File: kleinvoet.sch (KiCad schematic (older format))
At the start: 35 parts, among them CN1 Conn_01x06, CN2 Conn_01x10, CN3 Conn_01x08, J1 Conn_ST_STDC14, SW1 RESET, U1 STM32F446RETx, U2 W25Q128JVS, Y1 12 MHz, Y2 32.768 kHz

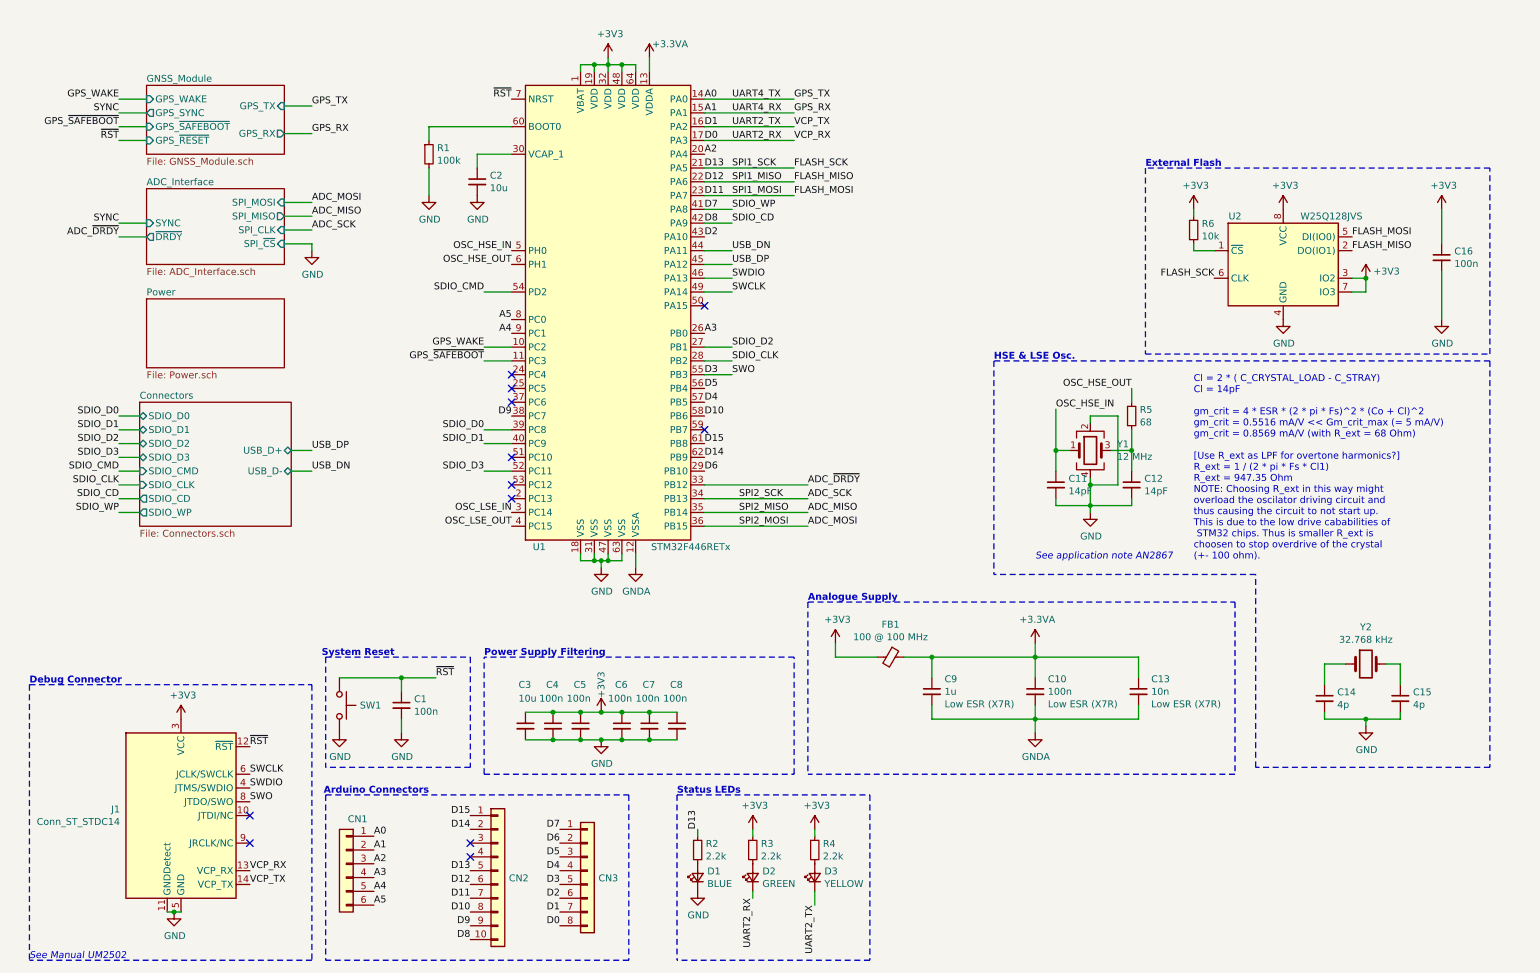
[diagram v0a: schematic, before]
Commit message: Assign footprints for all components
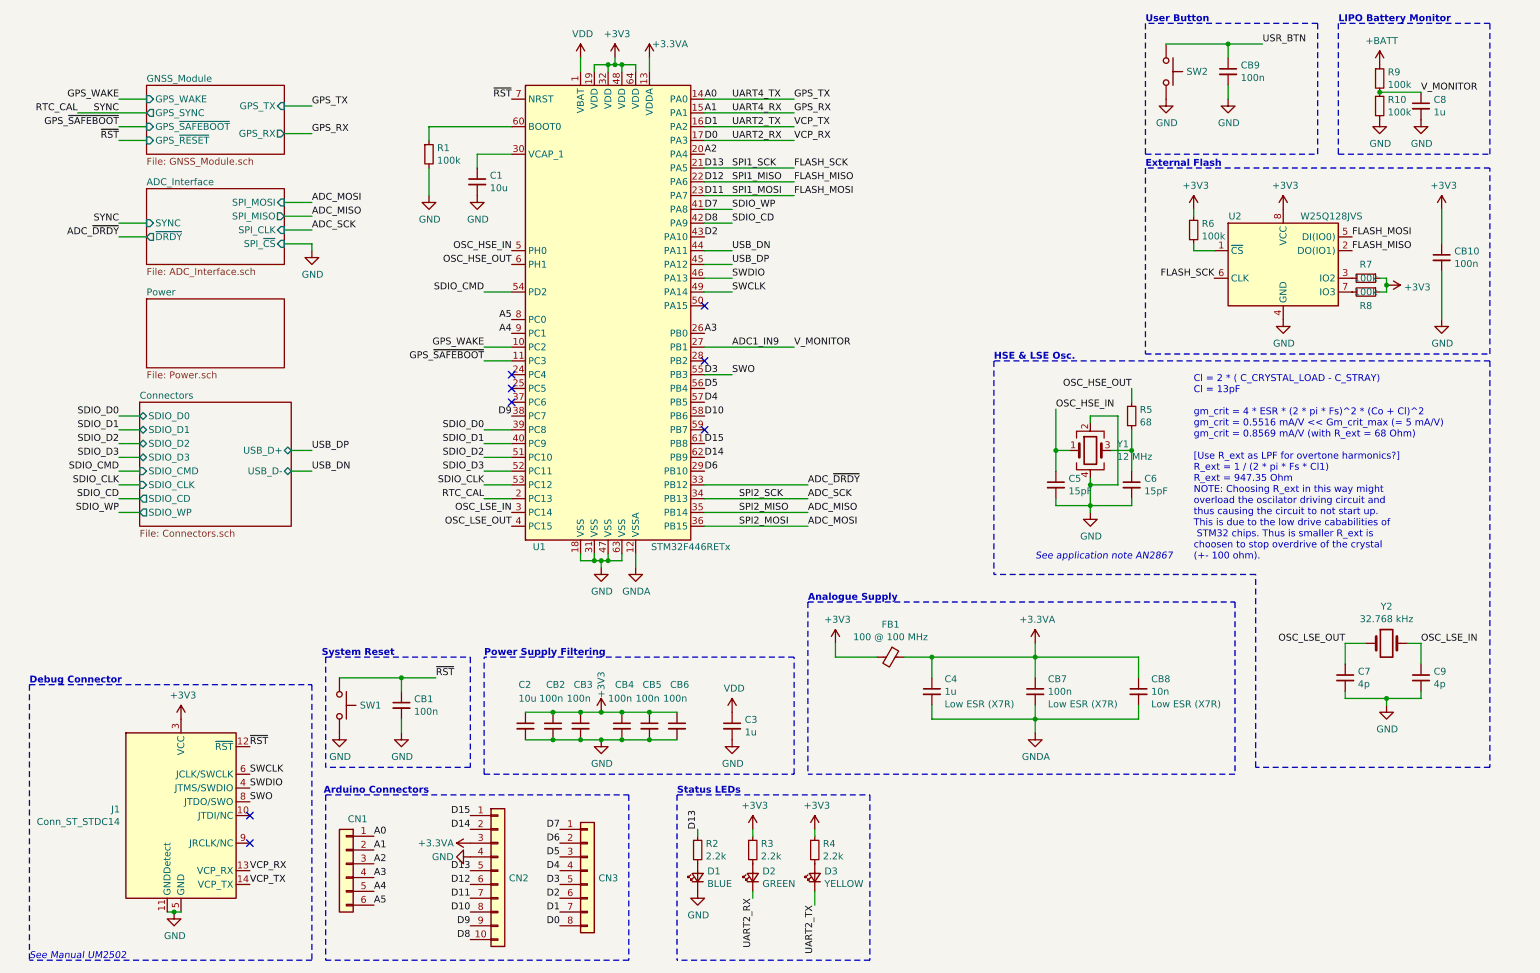
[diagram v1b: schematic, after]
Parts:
- added C3, C8: 1u, Capacitor_SMD:C_0603_1608Metric_Pad1.05x0.95mm_HandSolder, symbol Device:C_Small
- added CB9: 100n, Capacitor_SMD:C_0603_1608Metric_Pad1.05x0.95mm_HandSolder, symbol Device:C_Small
- added R10, R7, R8, R9: 100k, Resistor_SMD:R_0603_1608Metric_Pad1.05x0.95mm_HandSolder, symbol Device:R_Small
- added SW2: RESET, grootvoet:SW_SPST_PTS647, symbol Switch:SW_Push
- C1: renamed from C2; footprint (none) -> Capacitor_SMD:C_0805_2012Metric_Pad1.15x1.40mm_HandSolder; MPN (none) -> C0805C106K9PACTU; Mfr. (none) -> KEMET
- C2: renamed from C3; footprint (none) -> Capacitor_SMD:C_0805_2012Metric_Pad1.15x1.40mm_HandSolder; MPN (none) -> C0805C106K9PACTU; Mfr. (none) -> KEMET
- C4: renamed from C9; footprint (none) -> Capacitor_SMD:C_0603_1608Metric_Pad1.05x0.95mm_HandSolder; MPN (none) -> C0603C105K8RACTU; Mfr. (none) -> KEMET
- C5: renamed from C11; value 14pF -> 15pF; footprint (none) -> Capacitor_SMD:C_0603_1608Metric_Pad1.05x0.95mm_HandSolder; MPN (none) -> C0603C150J5GACTU; Mfr. (none) -> KEMET
- C6: renamed from C12; value 14pF -> 15pF; footprint (none) -> Capacitor_SMD:C_0603_1608Metric_Pad1.05x0.95mm_HandSolder; MPN (none) -> C0603C150J5GACTU; Mfr. (none) -> KEMET
- C7: renamed from C14; footprint (none) -> Capacitor_SMD:C_0603_1608Metric_Pad1.05x0.95mm_HandSolder; MPN (none) -> C1608C0G1H040C080AA; Mfr. (none) -> TDK
- C9: renamed from C15; footprint (none) -> Capacitor_SMD:C_0603_1608Metric_Pad1.05x0.95mm_HandSolder; MPN (none) -> C1608C0G1H040C080AA; Mfr. (none) -> TDK
- CB1: renamed from C1; footprint (none) -> Capacitor_SMD:C_0603_1608Metric_Pad1.05x0.95mm_HandSolder; MPN (none) -> C0603C104M5RACTU; Mfr. (none) -> KEMET
- CB10: renamed from C16; footprint (none) -> Capacitor_SMD:C_0603_1608Metric_Pad1.05x0.95mm_HandSolder; MPN (none) -> C0603C104M5RACTU; Mfr. (none) -> KEMET
- CB2: renamed from C4; footprint (none) -> Capacitor_SMD:C_0603_1608Metric_Pad1.05x0.95mm_HandSolder; MPN (none) -> C0603C104M5RACTU; Mfr. (none) -> KEMET
- CB3: renamed from C5; footprint (none) -> Capacitor_SMD:C_0603_1608Metric_Pad1.05x0.95mm_HandSolder; MPN (none) -> C0603C104M5RACTU; Mfr. (none) -> KEMET
- CB4: renamed from C6; footprint (none) -> Capacitor_SMD:C_0603_1608Metric_Pad1.05x0.95mm_HandSolder; MPN (none) -> C0603C104M5RACTU; Mfr. (none) -> KEMET
- CB5: renamed from C7; footprint (none) -> Capacitor_SMD:C_0603_1608Metric_Pad1.05x0.95mm_HandSolder; MPN (none) -> C0603C104M5RACTU; Mfr. (none) -> KEMET
- CB6: renamed from C8; footprint (none) -> Capacitor_SMD:C_0603_1608Metric_Pad1.05x0.95mm_HandSolder; MPN (none) -> C0603C104M5RACTU; Mfr. (none) -> KEMET
- CB7: renamed from C10; footprint (none) -> Capacitor_SMD:C_0603_1608Metric_Pad1.05x0.95mm_HandSolder; MPN (none) -> C0603C104M5RACTU; Mfr. (none) -> KEMET
- CB8: renamed from C13; footprint (none) -> Capacitor_SMD:C_0603_1608Metric_Pad1.05x0.95mm_HandSolder; MPN (none) -> C0603C103J5RACTU; Mfr. (none) -> KEMET
- CN1: footprint (none) -> Connector_PinHeader_2.54mm:PinHeader_1x06_P2.54mm_Vertical
- CN2: footprint (none) -> Connector_PinHeader_2.54mm:PinHeader_1x10_P2.54mm_Vertical
- CN3: footprint (none) -> Connector_PinHeader_2.54mm:PinHeader_1x08_P2.54mm_Vertical
- D1: footprint (none) -> LED_SMD:LED_0603_1608Metric_Pad1.05x0.95mm_HandSolder; MPN (none) -> SMLD12BN1WT86; Mfr. (none) -> ROHM Semiconductor
- D2: footprint (none) -> LED_SMD:LED_0603_1608Metric_Pad1.05x0.95mm_HandSolder;  MPN (none) -> SMLD12EN1WT86; Mfr. (none) -> ROHM Semiconductor
- D3: footprint (none) -> LED_SMD:LED_0603_1608Metric_Pad1.05x0.95mm_HandSolder; MPN (none) -> SML-D12Y8WT86C; Mfr. (none) -> ROHM Semiconductor
- FB1: footprint (none) -> Inductor_SMD:L_0603_1608Metric_Pad1.05x0.95mm_HandSolder; MPN (none) -> BLM18KG101TZ1D; Mfr. (none) -> Murata Semiconductor
- J1: footprint (none) -> Connector_PinHeader_1.27mm:PinHeader_2x07_P1.27mm_Vertical; MPN (none) -> M50-055023W0445; Mfr. (none) -> Harwin
- R1: footprint (none) -> Resistor_SMD:R_0603_1608Metric_Pad1.05x0.95mm_HandSolder; MPN (none) -> RC0603FR-07100KL; Mfr. (none) -> Yageo
- R2: footprint (none) -> Resistor_SMD:R_0603_1608Metric_Pad1.05x0.95mm_HandSolder; MPN (none) -> RC0603FR-072K2L; Mfr. (none) -> Yageo
- R3: footprint (none) -> Resistor_SMD:R_0603_1608Metric_Pad1.05x0.95mm_HandSolder; MFN (none) -> RC0603FR-072K2L; Mfr. (none) -> Yageo
- R4: footprint (none) -> Resistor_SMD:R_0603_1608Metric_Pad1.05x0.95mm_HandSolder
- R5: footprint (none) -> Resistor_SMD:R_0603_1608Metric_Pad1.05x0.95mm_HandSolder; MPN (none) -> RC0603FR-1068RL; Mfr. (none) -> Yageo
- R6: value 10k -> 100k; footprint (none) -> Resistor_SMD:R_0603_1608Metric_Pad1.05x0.95mm_HandSolder; MPN (none) -> RC0603FR-07100KL; Mfr. (none) -> Yageo
- SW1: footprint (none) -> grootvoet:SW_SPST_PTS647; MPN (none) -> PTS647SN50SMTR2LFS; Mfr. (none) -> C&K
- U2: footprint Package_SO:SOIC-8_5.23x5.23mm_P1.27mm -> grootvoet:SOIC-8_5.23x5.23mm_P1.27mm
- Y1: footprint (none) -> grootvoet:ECS-33B; Mfr. (none) -> ECS
- Y2: footprint (none) -> grootvoet:ECX-31B
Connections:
- net +3.3VA: now also CN2.3 (Pin_3)
- net +3V3: now also R7.1, R8.1; no longer U1.1 (VBAT), U2.3 (IO2), U2.7 (IO3)
- net GND: now also CN2.4 (Pin_4), C3.2, C8.2, CB9.2, R10.2, SW2.2
- net OSC_LSE_IN: now also C9.1, Y2.2
- net OSC_LSE_OUT: now also C7.1, Y2.1
- net SDIO_CLK: now also U1.53 (PC12); no longer U1.28 (PB2)
- net SDIO_D2: now also U1.51 (PC10); no longer U1.27 (PB1)
- net RTC_CAL: now reaches U1.2 (PC13)
- new net: R7.2, U2.3 (IO2)
- new net: R8.2, U2.7 (IO3)
- new net +BATT: R9.1
- new net ADC1_IN9: C8.1, R10.1, R9.2, U1.27 (PB1)
- new net USR_BTN: CB9.1, SW2.1
- new net VDD: C3.1, U1.1 (VBAT)
- no-connect marks 12 -> 8
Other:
- note added: "Cl = 2 * ( C_CRYSTAL_LOAD - C_STRAY)\nCl = 13pF\n\ngm_crit = 4 * ESR * (2 * pi * Fs)^2 * (Co + Cl)^2\ngm_crit = 0.5516 mA/V << Gm_crit_max (= 5 mA/V)\ngm_crit = 0.8569 mA/V (with R_ext = 68 Ohm)\n\n[Use R_ext as LPF for overtone harmonics?]\nR_ext = 1 / (2 * pi * Fs * Cl1)\nR_ext = 947.35 Ohm\nNOTE: Choosing R_ext in this way might \noverload the oscilator driving circuit and \nthus causing the c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"
- note added: "LIPO Battery Monitor"
- note added: "User Button"
- note removed: "Cl = 2 * ( C_CRYSTAL_LOAD - C_STRAY)\nCl = 14pF\n\ngm_crit = 4 * ESR * (2 * pi * Fs)^2 * (Co + Cl)^2\ngm_crit = 0.5516 mA/V << Gm_crit_max (= 5 mA/V)\ngm_crit = 0.8569 mA/V (with R_ext = 68 Ohm)\n\n[Use R_ext as LPF for overtone harmonics?]\nR_ext = 1 / (2 * pi * Fs * Cl1)\nR_ext = 947.35 Ohm\nNOTE: Choosing R_ext in this way might \noverload the oscilator driving circuit and \nthus causing the c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"
- moved on the sheet: C7, C9, Y2

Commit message: Change Mic Preamp
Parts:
- C3, C8: MPN (none) -> C0603C105K8RACTU; Mfr. (none) -> KEMET
- D2:  MPN SMLD12EN1WT86 -> (none); MPN (none) -> SMLD12EN1WT86
- FB1: value Ferrite_Bead_Small -> BLM18KG101TZ1D; Mfr. Murata Semiconductor -> Murata Electronics
- R3: MFN RC0603FR-072K2L -> (none); MPN (none) -> RC0603FR-072K2L
- R4: MPN (none) -> RC0603FR-072K2L; Mfr. (none) -> Yageo
- R7: MFN RC0603FR-07100KL -> (none); MPN (none) -> RC0603FR-07100KL
- SW2: MPN (none) -> PTS647SN50SMTR2LFS; Mfr. (none) -> C&K
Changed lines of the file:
@@
 AR Path="/5EE5ECAD/5F08CCF0" Ref="FB?"  Part="1"
 F 0 "FB1" V 6563 5500 50  0000 C CNN
-F 1 "Ferrite_Bead_Small" V 6654 5500 50  0001 C CNN
+F 1 "BLM18KG101TZ1D" V 6654 5500 50  0001 C CNN
 F 2 "Inductor_SMD:L_0603_1608Metric_Pad1.05x0.95mm_HandSolder" V 6730 5500 50  0001 C CNN
 F 3 "~" H 6800 5500 50  0001 C CNN
 F 4 "100 @ 100 MHz" V 6654 5500 50  0000 C CNN "Notes"
 F 5 "BLM18KG101TZ1D" V 6800 5500 50  0001 C CNN "MPN"
-F 6 "Murata Semiconductor" V 6800 5500 50  0001 C CNN "Mfr."
+F 6 "Murata Electronics" V 6800 5500 50  0001 C CNN "Mfr."
 	1    6800 5500
 	0    1    1    0
@@
 F 2 "Resistor_SMD:R_0603_1608Metric_Pad1.05x0.95mm_HandSolder" H 5800 6900 50  0001 C CNN
 F 3 "~" H 5800 6900 50  0001 C CNN
-F 4 "RC0603FR-072K2L" H 5800 6900 50  0001 C CNN "MFN"
+F 4 "" H 5800 6900 50  0001 C CNN "MFN"
 F 5 "Yageo" H 5800 6900 50  0001 C CNN "Mfr."
+F 6 "RC0603FR-072K2L" H 5800 6900 50  0001 C CNN "MPN"
 	1    5800 6900
 	1    0    0    -1
@@
 F 2 "LED_SMD:LED_0603_1608Metric_Pad1.05x0.95mm_HandSolder" V 5800 7100 50  0001 C CNN
 F 3 "~" V 5800 7100 50  0001 C CNN
-F 4 "SMLD12EN1WT86" V 5800 7100 50  0001 C CNN " MPN"
+F 4 "" V 5800 7100 50  0001 C CNN " MPN"
 F 5 "ROHM Semiconductor" V 5800 7100 50  0001 C CNN "Mfr."
+F 6 "SMLD12EN1WT86" H 5800 7100 50  0001 C CNN "MPN"
 	1    5800 7100
 	0    -1   -1   0
@@
 F 2 "Resistor_SMD:R_0603_1608Metric_Pad1.05x0.95mm_HandSolder" H 6250 6900 50  0001 C CNN
 F 3 "~" H 6250 6900 50  0001 C CNN
+F 4 "RC0603FR-072K2L" H 6250 6900 50  0001 C CNN "MPN"
+F 5 "Yageo" H 6250 6900 50  0001 C CNN "Mfr."
 	1    6250 6900
 	1    0    0    -1
@@
 F 2 "Resistor_SMD:R_0603_1608Metric_Pad1.05x0.95mm_HandSolder" H 10250 2750 50  0001 C CNN
 F 3 "~" H 10250 2750 50  0001 C CNN
-F 4 "RC0603FR-07100KL" V 10250 2750 50  0001 C CNN "MFN"
+F 4 "" V 10250 2750 50  0001 C CNN "MFN"
 F 5 "Yageo" V 10250 2750 50  0001 C CNN "Mfr."
+F 6 "RC0603FR-07100KL" H 10250 2750 50  0001 C CNN "MPN"
 	1    10250 2750
 	0    1    1    0
@@
 F 2 "Capacitor_SMD:C_0603_1608Metric_Pad1.05x0.95mm_HandSolder" H 5650 6000 50  0001 C CNN
 F 3 "~" H 5650 6000 50  0001 C CNN
+F 4 "C0603C105K8RACTU" H 5650 6000 50  0001 C CNN "MPN"
+F 5 "KEMET" H 5650 6000 50  0001 C CNN "Mfr."
 	1    5650 6000
 	1    0    0    -1
@@
 F 2 "Capacitor_SMD:C_0603_1608Metric_Pad1.05x0.95mm_HandSolder" H 10650 1500 50  0001 C CNN
 F 3 "~" H 10650 1500 50  0001 C CNN
+F 4 "C0603C105K8RACTU" H 10650 1500 50  0001 C CNN "MPN"
+F 5 "KEMET" H 10650 1500 50  0001 C CNN "Mfr."
 	1    10650 1500
 	1    0    0    -1
@@
 F 2 "grootvoet:SW_SPST_PTS647" H 8800 1450 50  0001 C CNN
 F 3 "~" H 8800 1450 50  0001 C CNN
+F 4 "PTS647SN50SMTR2LFS" H 8800 1250 50  0001 C CNN "MPN"
+F 5 "C&K" H 8800 1250 50  0001 C CNN "Mfr."
 	1    8800 1250
 	0    1    1    0

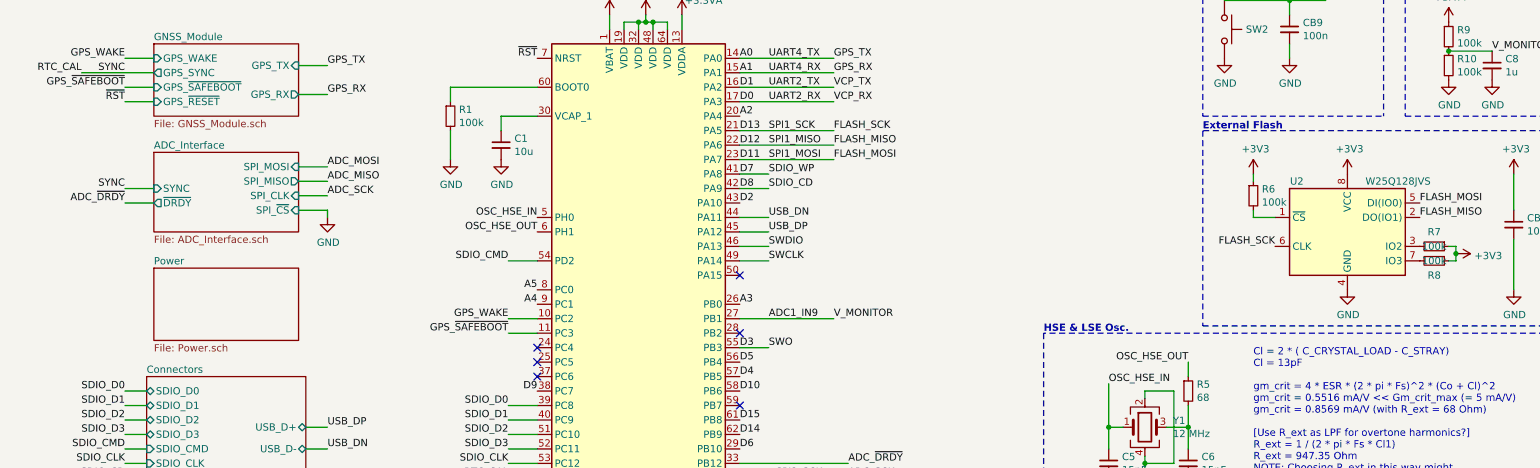
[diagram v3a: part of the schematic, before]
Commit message: Fix BOM ref
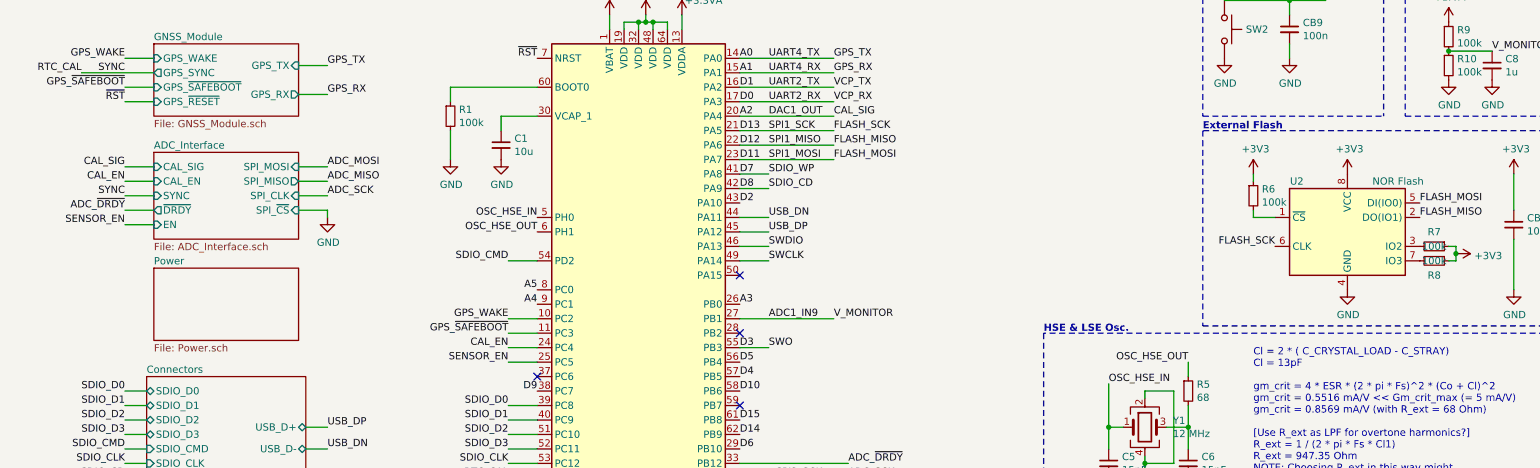
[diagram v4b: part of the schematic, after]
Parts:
- CN1: value Conn_01x06 -> Arduino_Conn
- CN2: value Conn_01x10 -> Arduino_Conn
- CN3: value Conn_01x08 -> Arduino_Conn
- U1: MPN (none) -> STM32F446RCT6; Mfr. (none) -> STMicroelectronics
- U2: value W25Q128JVS -> NOR Flash; MPN (none) -> W25Q16JVSNIQ; Mfr. (none) -> Winbond
- Y1: MPN ECS-120-12-33B-CWY-TR -> ECS-120-12-33-AEN-TR
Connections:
- net CAL_EN: now reaches U1.24 (PC4)
- net SENSOR_EN: now reaches U1.25 (PC5)
- no-connect marks 8 -> 6
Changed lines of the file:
@@
 $Descr A4 11693 8268
 encoding utf-8
-Sheet 1 15
+Sheet 1 17
 Title "Kleinvoet"
 Date "2020-06-11"
@@
 $EndDescr
 $Sheet
-S 1400 2100 1000 550
+S 1400 2100 1000 600
 U 5EE5ECAD
 F0 "ADC_Interface" 50
@@
 F3 "SPI_MISO" O R 2400 2300 50
 F4 "SPI_CLK" I R 2400 2400 50
-F5 "~DRDY" O L 1400 2450 50
+F5 "~DRDY" O L 1400 2500 50
 F6 "SPI_~CS" I R 2400 2500 50
-F7 "SYNC" I L 1400 2350 50
+F7 "SYNC" I L 1400 2400 50
+F8 "CAL_SIG" I L 1400 2200 50
+F9 "CAL_EN" I L 1400 2300 50
+F10 "EN" I L 1400 2600 50
 $EndSheet
 $Sheet
@@
 P 2850 7000
 F 0 "CN1" H 2768 7325 50  0000 C CNN
-F 1 "Conn_01x06" H 2768 7326 50  0001 C CNN
+F 1 "Arduino_Conn" H 2768 7326 50  0001 C CNN
 F 2 "Connector_PinHeader_2.54mm:PinHeader_1x06_P2.54mm_Vertical" H 2850 7000 50  0001 C CNN
 F 3 "~" H 2850 7000 50  0001 C CNN
@@
 P 3950 7050
 F 0 "CN2" H 4030 6996 50  0000 L CNN
-F 1 "Conn_01x10" H 4030 6951 50  0001 L CNN
+F 1 "Arduino_Conn" H 4030 6951 50  0001 L CNN
 F 2 "Connector_PinHeader_2.54mm:PinHeader_1x10_P2.54mm_Vertical" H 3950 7050 50  0001 C CNN
 F 3 "~" H 3950 7050 50  0001 C CNN
@@
 P 4600 7050
 F 0 "CN3" H 4680 6996 50  0000 L CNN
-F 1 "Conn_01x08" H 4680 6951 50  0001 L CNN
+F 1 "Arduino_Conn" H 4680 6951 50  0001 L CNN
 F 2 "Connector_PinHeader_2.54mm:PinHeader_1x08_P2.54mm_Vertical" H 4600 7050 50  0001 C CNN
 F 3 "~" H 4600 7050 50  0001 C CNN
@@
 F 2 "Package_QFP:LQFP-64_10x10mm_P0.5mm" H 4150 1250 50  0001 R CNN
 F 3 "http://www.st.com/st-web-ui/static/active/en/resource/technical/document/datasheet/DM00141306.pdf" H 4750 2950 50  0001 C CNN
+F 4 "STM32F446RCT6" H 4750 2950 50  0001 C CNN "MPN"
+F 5 "STMicroelectronics" H 4750 2950 50  0001 C CNN "Mfr."
 	1    4750 2950
 	1    0    0    -1
@@
 F 2 "grootvoet:ECS-33B" H 8250 4000 50  0001 C CNN
 F 3 "https://www.mouser.co.za/datasheet/2/122/ECS-33B-1649459.pdf" H 8250 4000 50  0001 C CNN
-F 4 "ECS-120-12-33B-CWY-TR" H 8250 4000 50  0001 C CNN "MPN"
+F 4 "ECS-120-12-33-AEN-TR" H 8250 4000 50  0001 C CNN "MPN"
 F 5 "ECS" H 8250 4000 50  0001 C CNN "Mfr."
 	1    8250 4000
@@
 P 9650 2650
 F 0 "U2" H 9300 3000 50  0000 C CNN
-F 1 "W25Q128JVS" H 10000 3000 50  0000 C CNN
+F 1 "NOR Flash" H 10000 3000 50  0000 C CNN
 F 2 "grootvoet:SOIC-8_5.23x5.23mm_P1.27mm" H 9650 2650 50  0001 C CNN
 F 3 "http://www.winbond.com/resource-files/w25q128jv_dtr%20revc%2003272018%20plus.pdf" H 9650 2650 50  0001 C CNN
+F 4 "W25Q16JVSNIQ" H 9650 2650 50  0001 C CNN "MPN"
+F 5 "Winbond" H 9650 2650 50  0001 C CNN "Mfr."
 	1    9650 2650
 	1    0    0    -1
@@
 Text Label 1200 1550 2    50   ~ 0
 SYNC
-Text Label 1200 2350 2    50   ~ 0
+Text Label 1200 2400 2    50   ~ 0
 SYNC
 Wire Wire Line
-	1200 2350 1400 2350
+	1200 2400 1400 2400
 Text Label 6200 4250 0    50   ~ 0
 ADC_~DRDY
 Wire Wire Line
 	6200 4250 5450 4250
-Text Label 1200 2450 2    50   ~ 0
+Text Label 1200 2500 2    50   ~ 0
 ADC_~DRDY
 Wire Wire Line
-	1200 2450 1400 2450
+	1200 2500 1400 2500
 Text Label 5650 1950 0    50   ~ 0
 SPI1_SCK
@@
 NoConn ~ 5450 3850
 NoConn ~ 4050 3650
-NoConn ~ 4050 3550
-NoConn ~ 4050 3450
 Text Label 10650 5400 0    50   ~ 0
 OSC_LSE_IN
@@
 Text Label 3850 3950 2    50   ~ 0
 SDIO_D1
+Text Label 6100 1850 0    50   ~ 0
+CAL_SIG
+Wire Wire Line
+	6100 1850 5450 1850
+Text Label 5650 1850 0    50   ~ 0
+DAC1_OUT
+Text Label 3850 3450 2    50   ~ 0
+CAL_EN
+Wire Wire Line
+	4050 3450 3850 3450
+Text Label 3850 3550 2    50   ~ 0
+SENSOR_EN
+Wire Wire Line
+	3850 3550 4050 3550
+Text Label 1200 2300 2    50   ~ 0
+CAL_EN
+Wire Wire Line
+	1200 2300 1400 2300
+Text Label 1200 2200 2    50   ~ 0
+CAL_SIG
+Wire Wire Line
+	1200 2200 1400 2200
+Text Label 1200 2600 2    50   ~ 0
+SENSOR_EN
+Wire Wire Line
+	1200 2600 1400 2600
 $EndSCHEMATC
